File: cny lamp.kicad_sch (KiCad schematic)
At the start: 26 parts, among them Q1 NX6008NBKWX, SW1 MHSS1104, U1 TC75W56, U2 74HC164, U3 74HC164, U4 Rabbit

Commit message: Label schematic
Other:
- note added: "Brief hold"
- note added: "Generate 50% duty square wave at ~1s period."
- note added: "Generate a rough triangle wave for outer "breathing" effect."
- note added: "Inverter"
- note added: "Power On Reset"
- note added: "Rabbit Fill-Empty chase effect."
- note added: "See Example: https://www.ti.com/lit/an/snoa998/snoa998.pdf"
- moved on the sheet: C1, U1C
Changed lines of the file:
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@@
   (junction (at 140.97 63.5) (diameter 0) (color 0 0 0 0)
   )
-  (junction (at 59.69 83.82) (diameter 0) (color 0 0 0 0)
+  (junction (at 40.64 34.29) (diameter 0) (color 0 0 0 0)
   )
   (wire (pts (xy 149.86 44.45) (xy 140.97 44.45))
@@
     (stroke (width 0) (type default) (color 0 0 0 0))
   )
-  (wire (pts (xy 59.69 81.28) (xy 59.69 83.82))
+  (wire (pts (xy 40.64 31.75) (xy 40.64 34.29))
     (stroke (width 0) (type default) (color 0 0 0 0))
   )
@@
     (stroke (width 0) (type default) (color 0 0 0 0))
   )
-  (wire (pts (xy 49.53 83.82) (xy 59.69 83.82))
-    (stroke (width 0) (type default) (color 0 0 0 0))
-  )
-  (wire (pts (xy 49.53 91.44) (xy 49.53 100.33))
+  (wire (pts (xy 30.48 34.29) (xy 40.64 34.29))
+    (stroke (width 0) (type default) (color 0 0 0 0))
+  )
+  (wire (pts (xy 30.48 41.91) (xy 30.48 50.8))
     (stroke (width 0) (type default) (color 0 0 0 0))
   )
@@
     (stroke (width 0) (type default) (color 0 0 0 0))
   )
-  (wire (pts (xy 59.69 100.33) (xy 59.69 99.06))
+  (wire (pts (xy 40.64 50.8) (xy 40.64 49.53))
     (stroke (width 0) (type default) (color 0 0 0 0))
   )
@@
   (wire (pts (xy 151.13 142.24) (xy 160.02 142.24))
     (stroke (width 0) (type default) (color 0 0 0 0))
+  )
+  (text "Generate 50% duty square wave\nat ~1s period." (at 78.74 63.5 0)
+    (effects (font (size 1.27 1.27)) (justify left bottom))
+  )
+  (text "Brief hold" (at 143.51 90.17 0)
+    (effects (font (size 1.27 1.27)) (justify left bottom))
+  )
+  (text "Rabbit Fill-Empty chase effect." (at 144.78 31.75 0)
+    (effects (font (size 1.27 1.27)) (justify left bottom))
+  )
+  (text "Power On Reset" (at 69.85 128.27 0)
+    (effects (font (size 1.27 1.27)) (justify left bottom))
+  )
+  (text "See Example:\nhttps://www.ti.com/lit/an/snoa998/snoa998.pdf"
+    (at 63.5 21.59 0)
+    (effects (font (size 1.27 1.27)) (justify left bottom))
+  )
+  (text "Generate a rough triangle wave\nfor outer \"breathing\" effect."
+    (at 143.51 127 0)
+    (effects (font (size 1.27 1.27)) (justify left bottom))
+  )
+  (text "Inverter" (at 49.53 166.37 0)
+    (effects (font (size 1.27 1.27)) (justify left bottom))
   )
   (label "last_op_inv" (at 115.57 43.18 180)
@@
     (pin "2")
   )
-  (symbol (lib_id "Device:C") (at 49.53 87.63 0) (unit 1)
-    (in_bom yes) (on_board yes) (fields_autoplaced)
-    (property "Reference" "C1" (id 0) (at 53.34 86.3599 0)
-      (effects (font (size 1.27 1.27)) (justify left))
-    )
-    (property "Value" "1u" (id 1) (at 53.34 88.8999 0)
-      (effects (font (size 1.27 1.27)) (justify left))
-    )
-    (property "Footprint" "Capacitor_SMD:C_1206_3216Metric_Pad1.33x1.80mm_HandSolder" (id 2) (at 50.4952 91.44 0)
-      (effects (font (size 1.27 1.27)) hide)
-    )
-    (property "Datasheet" "~" (id 3) (at 49.53 87.63 0)
-      (effects (font (size 1.27 1.27)) hide)
-    )
-    (property "PN" "CL31B105KAHNNNE" (id 4) (at 49.53 87.63 0)
+  (symbol (lib_id "Device:C") (at 30.48 38.1 0) (unit 1)
+    (in_bom yes) (on_board yes) (fields_autoplaced)
+    (property "Reference" "C1" (id 0) (at 34.29 36.8299 0)
+      (effects (font (size 1.27 1.27)) (justify left))
+    )
+    (property "Value" "1u" (id 1) (at 34.29 39.3699 0)
+      (effects (font (size 1.27 1.27)) (justify left))
+    )
+    (property "Footprint" "Capacitor_SMD:C_1206_3216Metric_Pad1.33x1.80mm_HandSolder" (id 2) (at 31.4452 41.91 0)
+      (effects (font (size 1.27 1.27)) hide)
+    )
+    (property "Datasheet" "~" (id 3) (at 30.48 38.1 0)
+      (effects (font (size 1.27 1.27)) hide)
+    )
+    (property "PN" "CL31B105KAHNNNE" (id 4) (at 30.48 38.1 0)
       (effects (font (size 1.27 1.27)) hide)
     )
@@
     (pin "1")
   )
-  (symbol (lib_id "Library:TC75W56") (at 62.23 91.44 0) (unit 3)
-    (in_bom yes) (on_board yes) (fields_autoplaced)
-    (property "Reference" "U1" (id 0) (at 60.96 90.1699 0)
-      (effects (font (size 1.27 1.27)) (justify left))
-    )
-    (property "Value" "TC75W56" (id 1) (at 60.96 92.7099 0)
-      (effects (font (size 1.27 1.27)) (justify left))
-    )
-    (property "Footprint" "Package_SO:VSSOP-8_2.3x2mm_P0.5mm" (id 2) (at 62.23 91.44 0)
-      (effects (font (size 1.27 1.27)) hide)
-    )
-    (property "Datasheet" "https://toshiba.semicon-storage.com/info/TC75W56FU_datasheet_en_20171201.pdf?did=21013&prodName=TC75W56FU" (id 3) (at 62.23 82.55 0)
+  (symbol (lib_id "Library:TC75W56") (at 43.18 41.91 0) (unit 3)
+    (in_bom yes) (on_board yes) (fields_autoplaced)
+    (property "Reference" "U1" (id 0) (at 41.91 40.6399 0)
+      (effects (font (size 1.27 1.27)) (justify left))
+    )
+    (property "Value" "TC75W56" (id 1) (at 41.91 43.1799 0)
+      (effects (font (size 1.27 1.27)) (justify left))
+    )
+    (property "Footprint" "Package_SO:VSSOP-8_2.3x2mm_P0.5mm" (id 2) (at 43.18 41.91 0)
+      (effects (font (size 1.27 1.27)) hide)
+    )
+    (property "Datasheet" "https://toshiba.semicon-storage.com/info/TC75W56FU_datasheet_en_20171201.pdf?did=21013&prodName=TC75W56FU" (id 3) (at 43.18 33.02 0)
       (effects (font (size 1.27 1.27)) hide)
     )
@@
     (pin "1")
   )
-  (symbol (lib_id "power:VCC") (at 59.69 81.28 0) (unit 1)
-    (in_bom yes) (on_board yes) (fields_autoplaced)
-    (property "Reference" "#PWR07" (id 0) (at 59.69 85.09 0)
-      (effects (font (size 1.27 1.27)) hide)
-    )
-    (property "Value" "VCC" (id 1) (at 59.69 76.2 0))
-    (property "Footprint" "" (id 2) (at 59.69 81.28 0)
-      (effects (font (size 1.27 1.27)) hide)
-    )
-    (property "Datasheet" "" (id 3) (at 59.69 81.28 0)
+  (symbol (lib_id "power:VCC") (at 40.64 31.75 0) (unit 1)
+    (in_bom yes) (on_board yes) (fields_autoplaced)
+    (property "Reference" "#PWR07" (id 0) (at 40.64 35.56 0)
+      (effects (font (size 1.27 1.27)) hide)
+    )
+    (property "Value" "VCC" (id 1) (at 40.64 26.67 0))
+    (property "Footprint" "" (id 2) (at 40.64 31.75 0)
+      (effects (font (size 1.27 1.27)) hide)
+    )
+    (property "Datasheet" "" (id 3) (at 40.64 31.75 0)
       (effects (font (size 1.27 1.27)) hide)
     )
@@
     (pin "1")
   )
-  (symbol (lib_id "power:GND") (at 49.53 100.33 0) (unit 1)
-    (in_bom yes) (on_board yes) (fields_autoplaced)
-    (property "Reference" "#PWR03" (id 0) (at 49.53 106.68 0)
-      (effects (font (size 1.27 1.27)) hide)
-    )
-    (property "Value" "GND" (id 1) (at 49.53 105.41 0))
-    (property "Footprint" "" (id 2) (at 49.53 100.33 0)
-      (effects (font (size 1.27 1.27)) hide)
-    )
-    (property "Datasheet" "" (id 3) (at 49.53 100.33 0)
+  (symbol (lib_id "power:GND") (at 30.48 50.8 0) (unit 1)
+    (in_bom yes) (on_board yes) (fields_autoplaced)
+    (property "Reference" "#PWR03" (id 0) (at 30.48 57.15 0)
+      (effects (font (size 1.27 1.27)) hide)
+    )
+    (property "Value" "GND" (id 1) (at 30.48 55.88 0))
+    (property "Footprint" "" (id 2) (at 30.48 50.8 0)
+      (effects (font (size 1.27 1.27)) hide)
+    )
+    (property "Datasheet" "" (id 3) (at 30.48 50.8 0)
       (effects (font (size 1.27 1.27)) hide)
     )
@@
     (pin "9")
   )
-  (symbol (lib_id "power:GND") (at 59.69 100.33 0) (unit 1)
-    (in_bom yes) (on_board yes) (fields_autoplaced)
-    (property "Reference" "#PWR08" (id 0) (at 59.69 106.68 0)
-      (effects (font (size 1.27 1.27)) hide)
-    )
-    (property "Value" "GND" (id 1) (at 59.69 105.41 0))
-    (property "Footprint" "" (id 2) (at 59.69 100.33 0)
-      (effects (font (size 1.27 1.27)) hide)
-    )
-    (property "Datasheet" "" (id 3) (at 59.69 100.33 0)
-      (effects (font (size 1.27 1.27)) hide)
-    )
+  (symbol (lib_id "power:GND") (at 40.64 50.8 0) (unit 1)
+    (in_bom yes) (on_board yes) (fields_autoplaced)
+    (property "Reference" "#PWR08" (id 0) (at 40.64 57.15 0)
+      (effects (font (size 1.27 1.27)) hide)
+    )
+    (property "Value" "GND" (id 1) (at 40.64 55.88 0))
+    (property "Footprint" "" (id 2) (at 40.64 50.8 0)
+      (effects (font (size 1.27 1.27)) hide)
+    )
+    (property "Datasheet" "" (id 3) (at 40.64 50.8 0)
+      (effects (font (size 1.27 1.27)) hide)
+    )

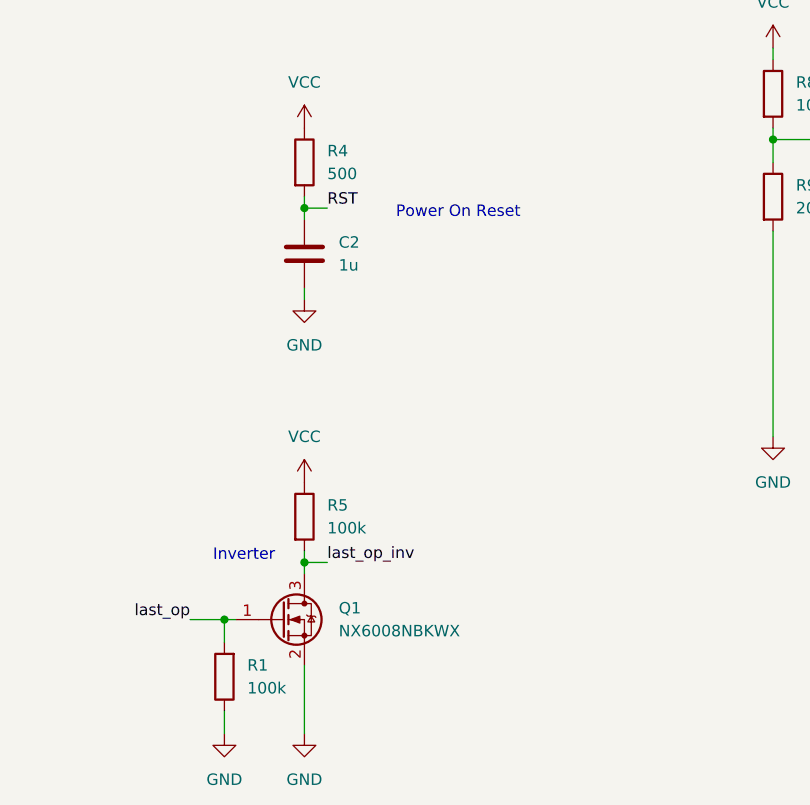
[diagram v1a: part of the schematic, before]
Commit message: Add BoM and complete board
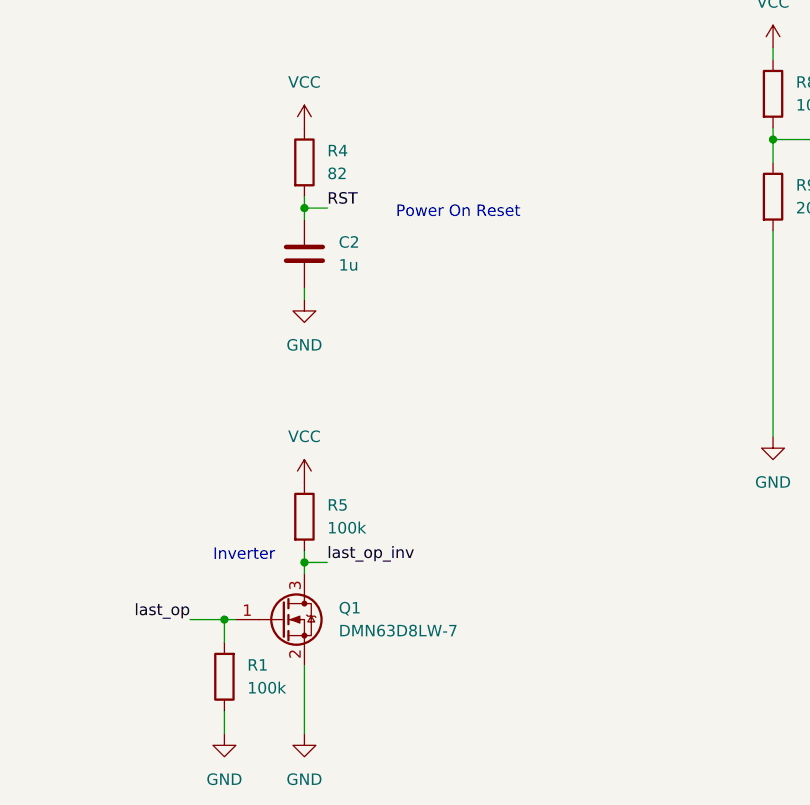
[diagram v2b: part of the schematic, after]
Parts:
- BT1: PN (none) -> Keystone_2468
- Q1: value NX6008NBKWX -> DMN63D8LW-7
- R4: value 500 -> 82
